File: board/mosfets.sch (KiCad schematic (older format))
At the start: 66 parts

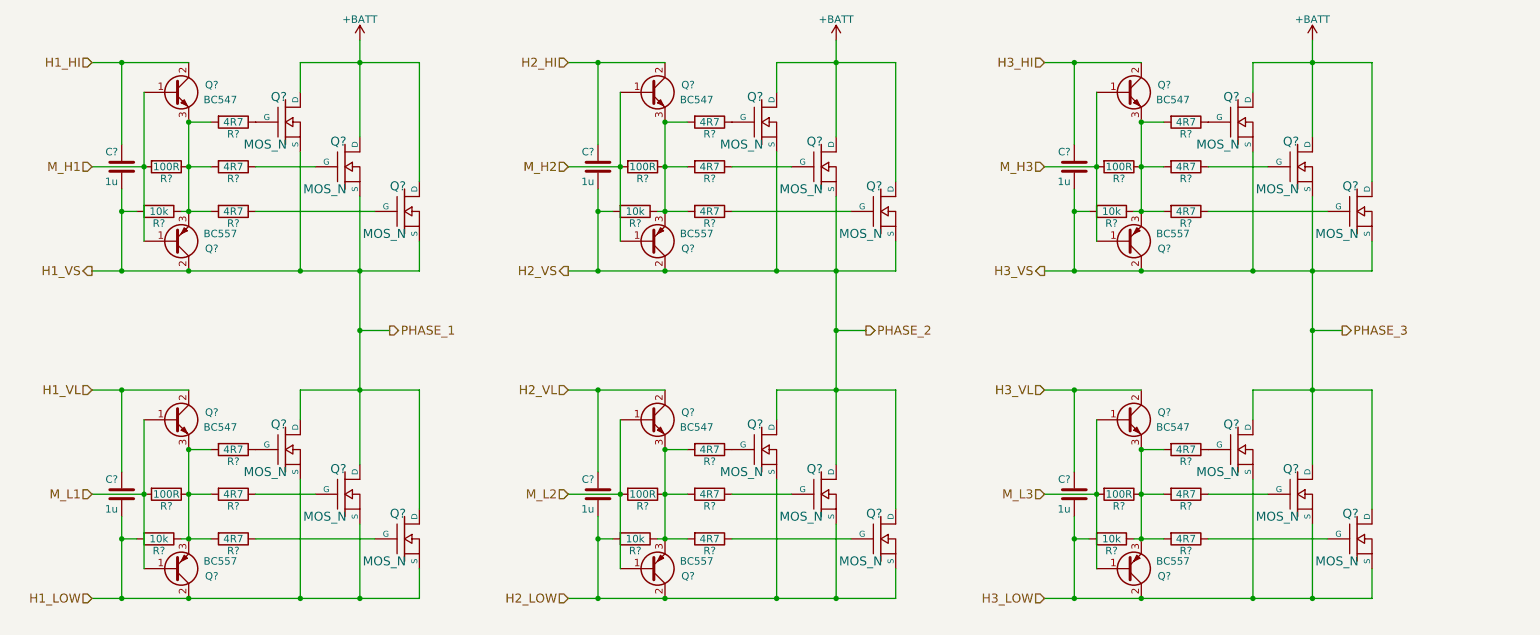
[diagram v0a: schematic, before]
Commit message: - implemented complementary transistor package - started layout
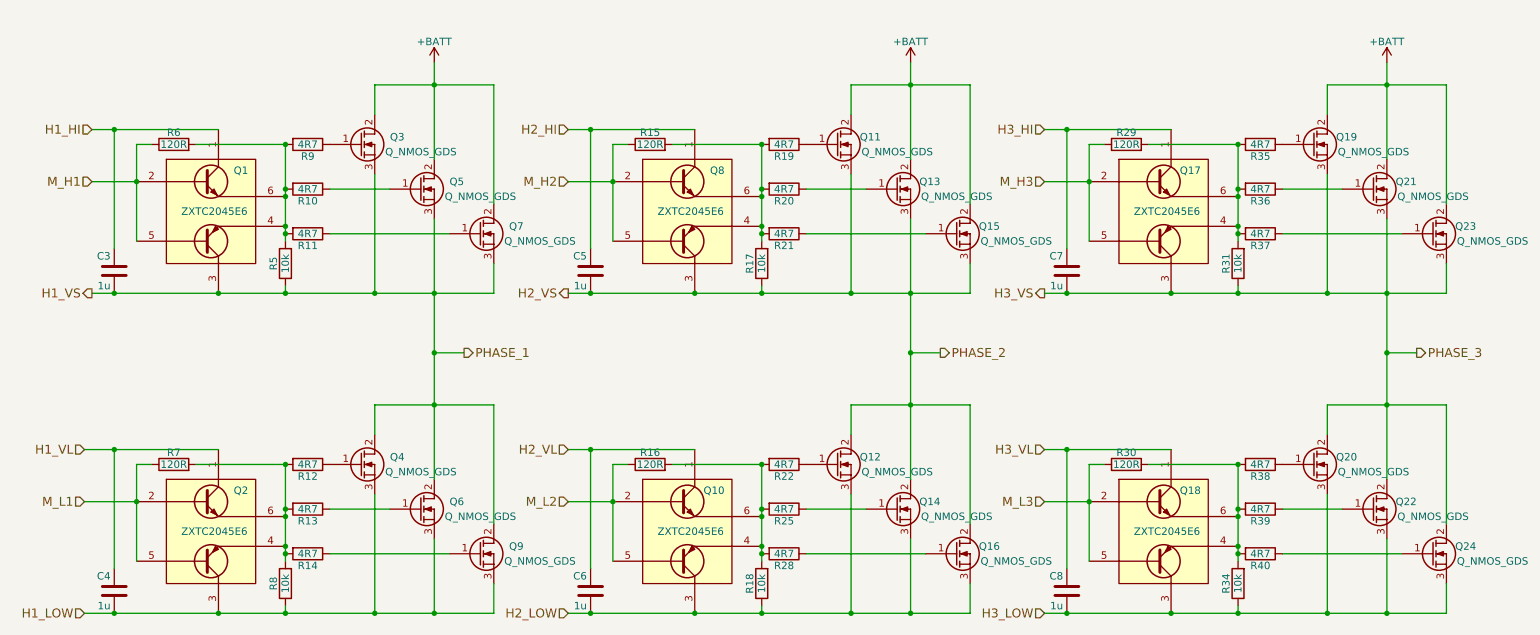
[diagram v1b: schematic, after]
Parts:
- removed C? (x5): 1u, symbol C
- removed Q? (x18): MOS_N, symbol MOS_N
- removed Q? (x6): BC547, symbol Q_NPN_BCE
- removed Q? (x6): BC557, symbol Q_PNP_BCE
- removed R? (x6): 100R, symbol R
- removed R? (x15): 4R7, symbol R
- removed R? (x5): 10k, symbol R
- added C4, C5, C6, C7, C8: 1u, Capacitors_SMD:C_0805, symbol C
- added Q1, Q10, Q17, Q18, Q2, Q8: ZXTC2045E6, TO_SOT_Packages_SMD:SOT-23-6, symbol ZXTC2045E6
- added Q11, Q12, Q13, Q14, Q15, Q16, Q19, Q20, Q21, Q22, Q23, Q24, Q3, Q4, Q5, Q6, Q7, Q9: Q_NMOS_GDS, alexmod:TO-264_flat_reverse, symbol Q_NMOS_GDS
- added R12, R13, R14, R19, R20, R21, R22, R25, R28, R35, R36, R37, R38, R39, R40: 4R7, Resistors_SMD:R_0805, symbol R
- added R15, R16, R29, R30, R6, R7: 120R, Resistors_SMD:R_0805, symbol R
- added R17, R18, R31, R34, R8: 10k, Resistors_SMD:R_0805, symbol R
- C3: renamed from C?; footprint (none) -> Capacitors_SMD:C_0805
- R10, R11, R5, R9: renamed from R?; footprint (none) -> Resistors_SMD:R_0805
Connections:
- net +BATT: now also Q11.2 (D), Q13.2 (D), Q15.2 (D), Q19.2 (D), Q21.2 (D), Q23.2 (D), Q3.2 (D), Q5.2 (D), Q7.2 (D)
- net H1_HI: now also Q1.1 (C1)
- net H1_LOW: now also C4.2, Q2.3 (C2), Q4.3 (S), Q6.3 (S), Q9.3 (S), R8.1
- net H1_VL: now also C4.1, Q2.1 (C1)
- net H1_VS: now also R5.1, Q1.3 (C2), Q3.3 (S), Q4.2 (D), Q5.3 (S), Q6.2 (D), Q7.3 (S), Q9.2 (D); no longer R5.2
- net H2_HI: now also C5.1, Q8.1 (C1)
- net H2_LOW: now also C6.2, Q10.3 (C2), Q12.3 (S), Q14.3 (S), Q16.3 (S), R18.1
- net H2_VL: now also C6.1, Q10.1 (C1)
- net H2_VS: now also C5.2, Q11.3 (S), Q12.2 (D), Q13.3 (S), Q14.2 (D), Q15.3 (S), Q16.2 (D), Q8.3 (C2), R17.1
- net H3_HI: now also C7.1, Q17.1 (C1)
- net H3_LOW: now also C8.2, Q18.3 (C2), Q20.3 (S), Q22.3 (S), Q24.3 (S), R34.1
- net H3_VL: now also C8.1, Q18.1 (C1)
- net H3_VS: now also C7.2, Q17.3 (C2), Q19.3 (S), Q20.2 (D), Q21.3 (S), Q22.2 (D), Q23.3 (S), Q24.2 (D), R31.1
- net M_H1: now also Q1.2 (B1), Q1.5 (B2), R6.1
- net M_H2: now also Q8.2 (B1), Q8.5 (B2), R15.1
- net M_H3: now also Q17.2 (B1), Q17.5 (B2), R29.1
- net M_L1: now also Q2.2 (B1), Q2.5 (B2), R7.1
- net M_L2: now also Q10.2 (B1), Q10.5 (B2), R16.1
- net M_L3: now also Q18.2 (B1), Q18.5 (B2), R30.1
- net at R9.1: now also Q3.1 (G)
- net at R10.1: now also Q5.1 (G)
- net at R11.1: now also Q7.1 (G)
- net at R10.2, R11.2, R9.2: now also R5.2, Q1.4 (E2), Q1.6 (E1), R6.2; no longer R5.1
- new net: Q22.1 (G), R39.1
- new net: Q18.4 (E2), Q18.6 (E1), R30.2, R34.2, R38.2, R39.2, R40.2
- new net: Q20.1 (G), R38.1
- new net: Q24.1 (G), R40.1
- new net: Q6.1 (G), R13.1
- new net: Q2.4 (E2), Q2.6 (E1), R12.2, R13.2, R14.2, R7.2, R8.2
- new net: Q4.1 (G), R12.1
- new net: Q9.1 (G), R14.1
- new net: Q13.1 (G), R20.1
- new net: Q8.4 (E2), Q8.6 (E1), R15.2, R17.2, R19.2, R20.2, R21.2
- new net: Q11.1 (G), R19.1
- new net: Q15.1 (G), R21.1
- new net: Q14.1 (G), R25.1
- new net: Q10.4 (E2), Q10.6 (E1), R16.2, R18.2, R22.2, R25.2, R28.2
- new net: Q12.1 (G), R22.1
- new net: Q16.1 (G), R28.1
- new net: Q21.1 (G), R36.1
- new net: Q17.4 (E2), Q17.6 (E1), R29.2, R31.2, R35.2, R36.2, R37.2
- new net: Q19.1 (G), R35.1
- new net: Q23.1 (G), R37.1
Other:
- moved on the sheet: C3, R10, R11, R5, R9
